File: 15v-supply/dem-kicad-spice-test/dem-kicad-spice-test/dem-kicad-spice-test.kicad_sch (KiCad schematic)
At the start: 23 parts, among them J1 Screw_Terminal_01x03

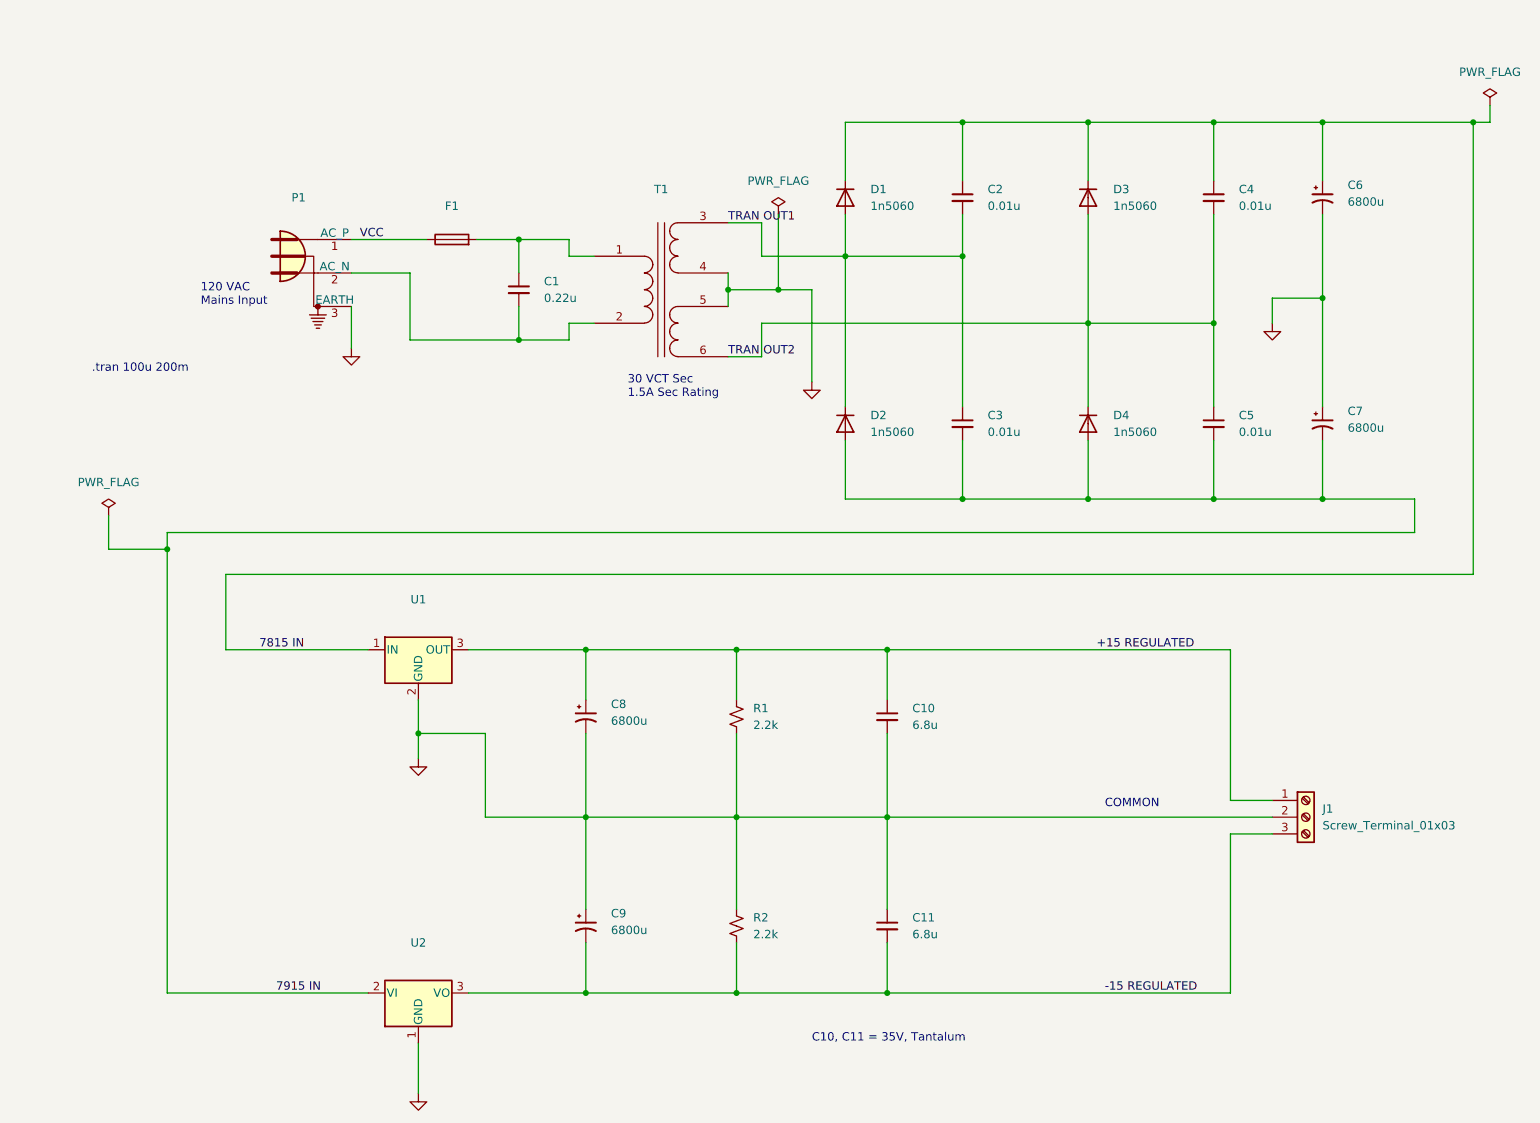
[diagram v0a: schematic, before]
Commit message: updates to the 15v-supply spice models
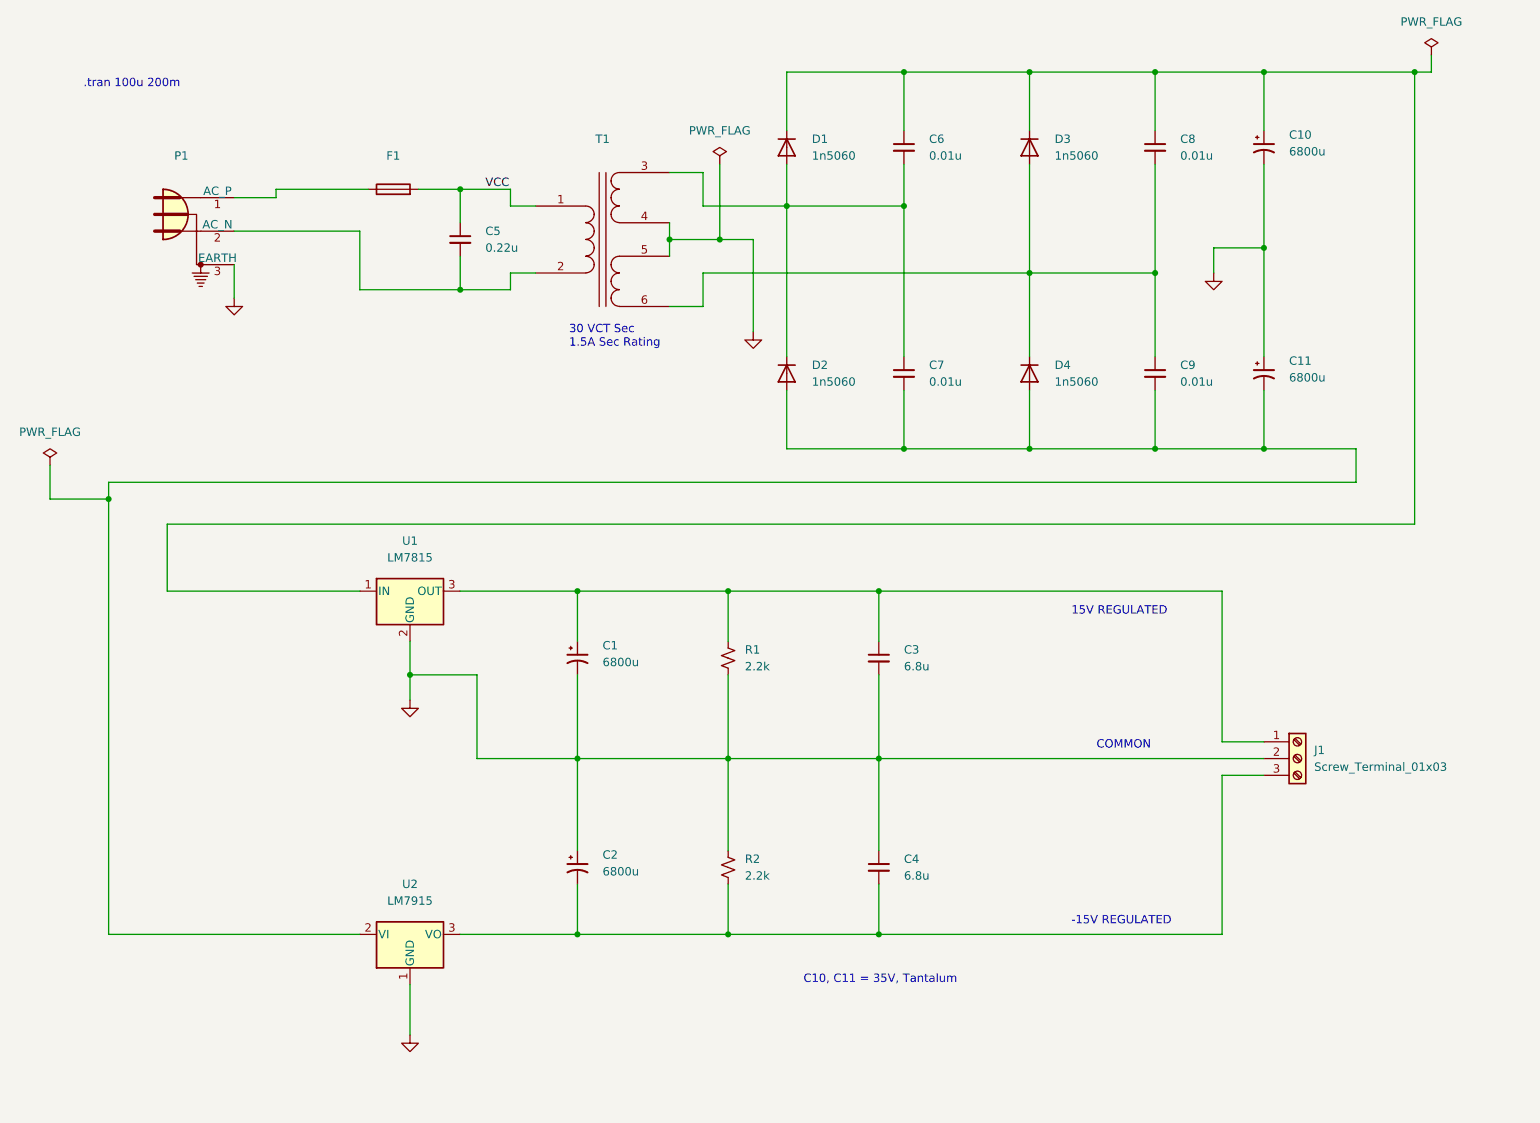
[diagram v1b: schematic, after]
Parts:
- removed C1: 0.22u, Capacitor_THT:C_Axial_L5.1mm_D3.1mm_P7.50mm_Horizontal, symbol Device:C_Small
- removed C10, C11: 6.8u, symbol Device:C_Small
- removed C2: 0.01u, symbol Device:C_Small
- removed C6, C7, C8, C9: 6800u, symbol Device:C_Polarized_Small_US
- added C1, C10, C11, C2: 6800u, symbol Device:C_Polarized_Small_US
- added C6, C7, C8, C9: 0.01u, symbol Device:C_Small
- C3, C4: value 0.01u -> 6.8u
- C5: value 0.01u -> 0.22u; footprint (none) -> Capacitor_THT:C_Axial_L5.1mm_D3.1mm_P7.50mm_Horizontal
- U1: value (none) -> LM7815
- U2: value (none) -> LM7915
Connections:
- net GND: now also C3.2, C4.1, C1.2, C10.2, C11.1, C2.1
- net VCC: now also C5.1, F1.2, T1.1 (AA); no longer F1.1, P1.1 (AC_P)
- net at P1.2 (AC_N), T1.2 (AB): now also C5.2
- net +15 REGULATED: no longer names the net of J1.1 (Pin_1), R1.1, U1.3 (OUT)
- net +15 REGULATED: now also C3.1, C1.1
- net -15 REGULATED: no longer names the net of J1.3 (Pin_3), R2.2, U2.3 (VO)
- net -15 REGULATED: now also C4.2, C2.2
- net 7815 IN: no longer names the net of D1.C, D3.C, U1.1 (IN)
- net 7815 IN: now also C10.1, C6.1, C8.1; no longer C4.1
- net 7915 IN: no longer names the net of D2.A, D4.A, U2.2 (VI)
- net 7915 IN: now also C11.2, C7.2, C9.2; no longer C3.2, C5.2
- net TRAN OUT1: no longer names the net of D1.A, D2.C, T1.3 (SA)
- net TRAN OUT1: now also C6.2, C7.1; no longer C3.1
- net TRAN OUT2: no longer names the net of D3.A, D4.C, T1.6 (SD)
- net TRAN OUT2: now also C8.2, C9.1; no longer C4.2, C5.1
- new net: F1.1, P1.1 (AC_P)
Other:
- note added: "-15V REGULATED"
- note added: "15V REGULATED"
- note removed: "120 VAC Mains Input"
- company: Andy McCann KA3KAF and Doug McCann KA3KAG -> (none)
- title: Dual Polarity 15V Supply -> (none)
